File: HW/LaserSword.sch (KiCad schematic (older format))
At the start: 28 parts, among them J1 Conn_02x05_Odd_Even, J2 Conn_01x05, J3 Conn_01x05, J4 Conn_01x05, Q1 Q_PNP_BEC, Q2 Q_PNP_BEC, U1 MMA7660FC, U2 DAC101S101, U3 MKE04Z8VWJ4

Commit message: First pass at layout
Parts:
- C1, C2, C3, C4, C5, C6, C7: footprint (none) -> Capacitors_SMD:C_0603_HandSoldering
- J1: value Conn_02x05_Odd_Even -> SWD; footprint (none) -> Pin_Headers:Pin_Header_Straight_2x05_Pitch1.27mm; digikey# (none) -> SAM9430-ND
- J2: value Conn_01x05 -> INPUTS; footprint (none) -> Pin_Headers:Pin_Header_Straight_1x05_Pitch1.00mm; MfrPart (none) -> SMH100-LPSE-Sxx-ST-BK; digikey# (none) -> S9215-ND
- J3: value Conn_01x05 -> OUTPUTS; footprint (none) -> Pin_Headers:Pin_Header_Straight_1x05_Pitch1.00mm; MfrPart (none) -> SMH100-LPSE-Sxx-ST-BK; digikey# (none) -> S9215-ND
- J4: value Conn_01x05 -> DEBUG; footprint (none) -> Pin_Headers:Pin_Header_Straight_1x05_Pitch1.00mm; MfrPart (none) -> SMH100-LPSE-Sxx-ST-BK; digikey# (none) -> S9215-ND
- Q1, Q2: footprint (none) -> TO_SOT_Packages_SMD:SOT-23; MfrPart (none) -> MMBT2907A; digikey# (none) -> MMBT2907ALT3GOSCT-ND
- R1, R10, R11, R12, R2, R3, R4, R5, R6, R7, R8, R9: footprint (none) -> Resistors_SMD:R_0603_HandSoldering
- U1: footprint MODULE -> dfn-10-3x3mm_pitch0:DFN-10_3x3mm_Pitch0.5mm; MfrPart (none) -> MMA7660FCT; digikey# (none) -> MMA7660FCT-ND
- U2: footprint MODULE -> TO_SOT_Packages_SMD:SOT-23-6_Handsoldering; MfrPart (none) -> DAC101S101CIMK/NOPB; digikey# (none) -> DAC101S101CIMK/NOPBCT-ND
- U3: footprint MODULE -> Housings_SOIC:SO-20_12.8x7.5mm_Pitch1.27mm; MfrPart (none) -> MKE04Z8VWJ4; digikey# (none) -> MKE04Z8VWJ4-ND

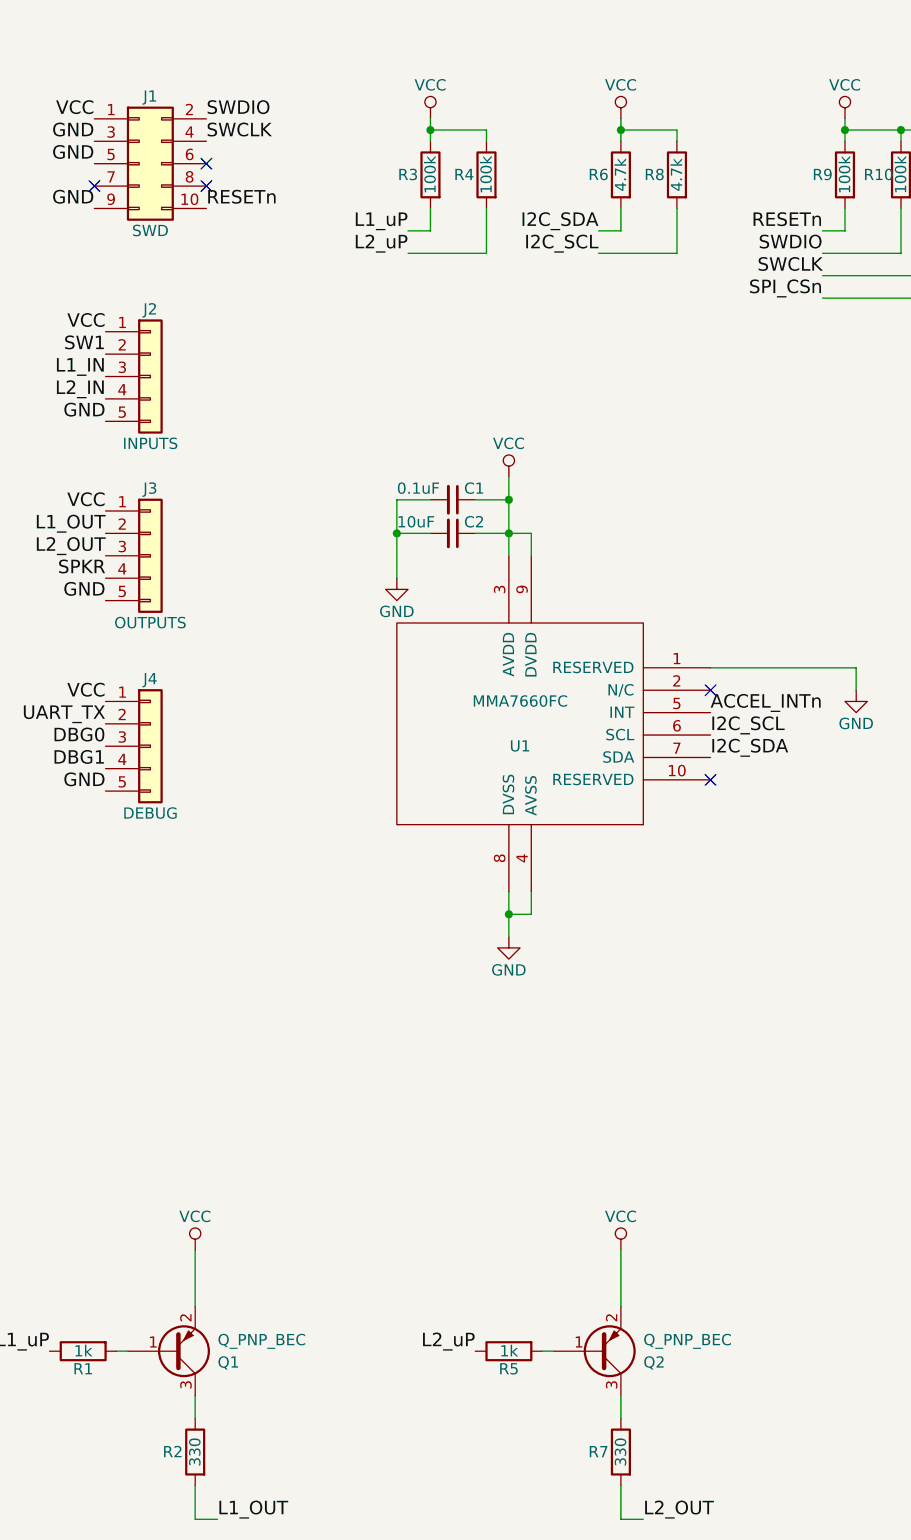
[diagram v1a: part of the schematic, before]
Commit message: Refactor to use NPN
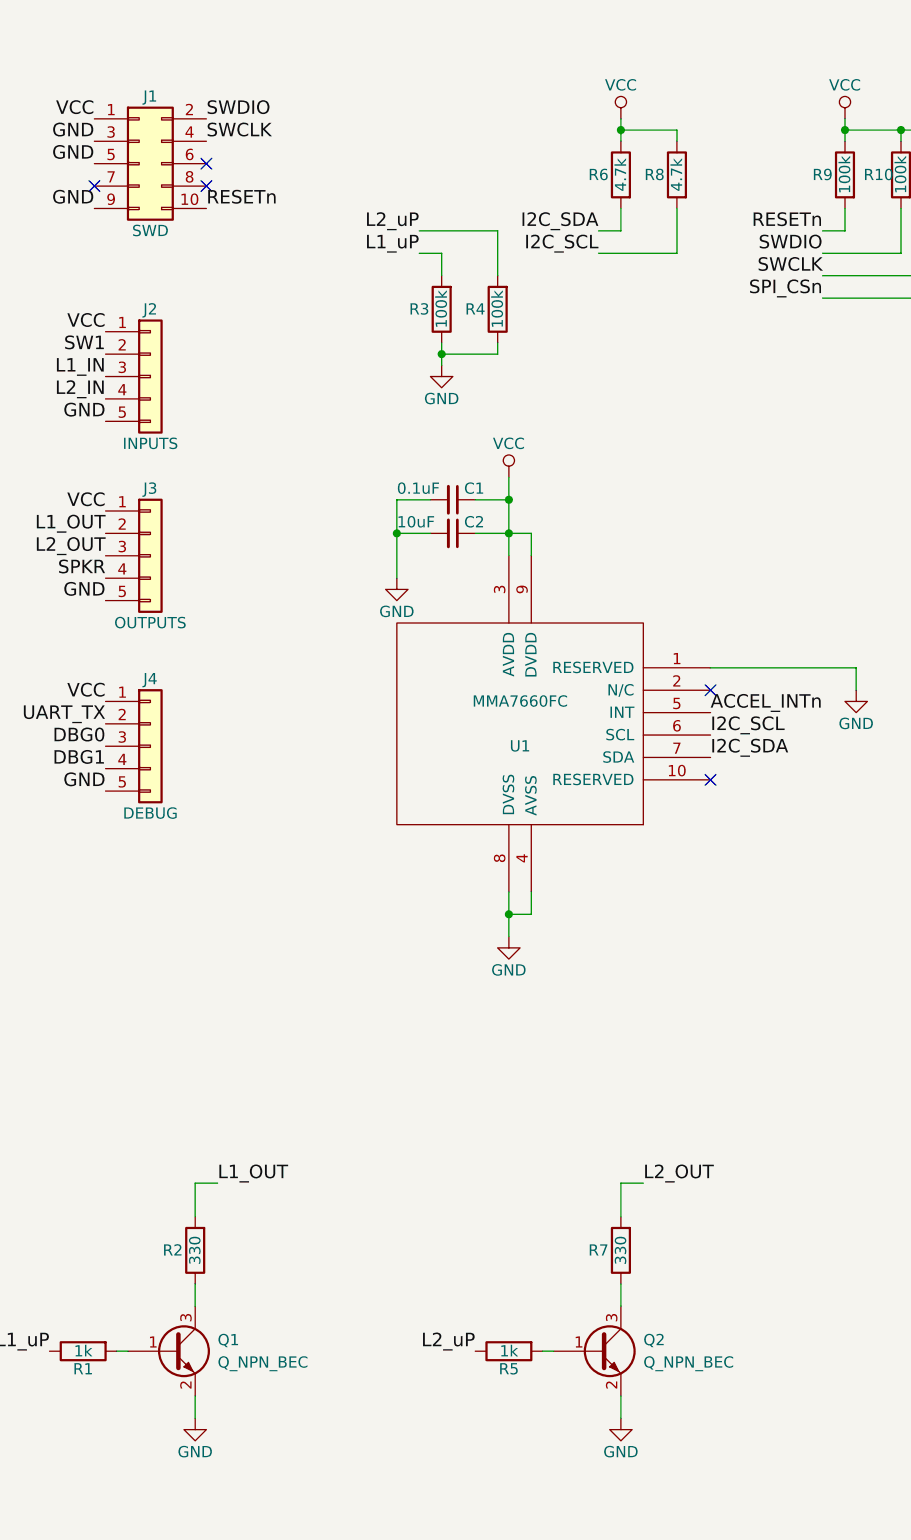
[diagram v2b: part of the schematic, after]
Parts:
- removed Q1, Q2: Q_PNP_BEC, TO_SOT_Packages_SMD:SOT-23, symbol Q_PNP_BEC
- added Q1, Q2: Q_NPN_BEC, TO_SOT_Packages_SMD:SOT-23, symbol Q_NPN_BEC
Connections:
- net GND: now also R3.1, R4.1, Q1.2 (E), Q2.2 (E)
- net VCC: no longer R3.1, R4.1
- net at R2.1: now also Q1.3 (C)
- net at R1.2: now also Q1.1 (B)
- net at R7.1: now also Q2.3 (C)
- net at R5.2: now also Q2.1 (B)
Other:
- moved on the sheet: R2, R3, R4, R7

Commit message: Rebuilt with dual opamp, diff. speaker drive
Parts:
- added C8: 10uF, Capacitors_SMD:C_0603_HandSoldering, symbol C_Small
- added MH1: MH1, MountingHole_2.2mm_M2, symbol TEST_1P
- added R13, R14, R15, R16: 4.7k, Resistors_SMD:R_0603_HandSoldering, symbol R
- added U4: LM358, Housings_SOIC:SOIC-8_3.9x4.9mm_Pitch1.27mm, symbol LM358
- C5: value 10uF -> 0.1uF
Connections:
- net GND: now also C5.2, C8.2, R15.1, U4.4 (V-); no longer J3.5 (Pin_5)
- net VCC: now also C5.1, C8.1, R14.2, U4.8 (V+)
- net DAC_OUT: now reaches U2.1 (VOUT)
- net DAC_OUT: now also R13.2, U4.3 (+); no longer C5.2
- net SPKR renamed SPKR_P
- net SPKR_P: now also U4.1, U4.2 (-); no longer C5.1
- new net: R14.1, R15.2, U4.5 (+)
- new net: R13.1, R16.2, U4.6 (-)
- new net SPKR_N: J3.5 (Pin_5), R16.1, U4.7
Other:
- moved on the sheet: C3, C4, U2
